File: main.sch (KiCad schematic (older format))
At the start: 0 parts

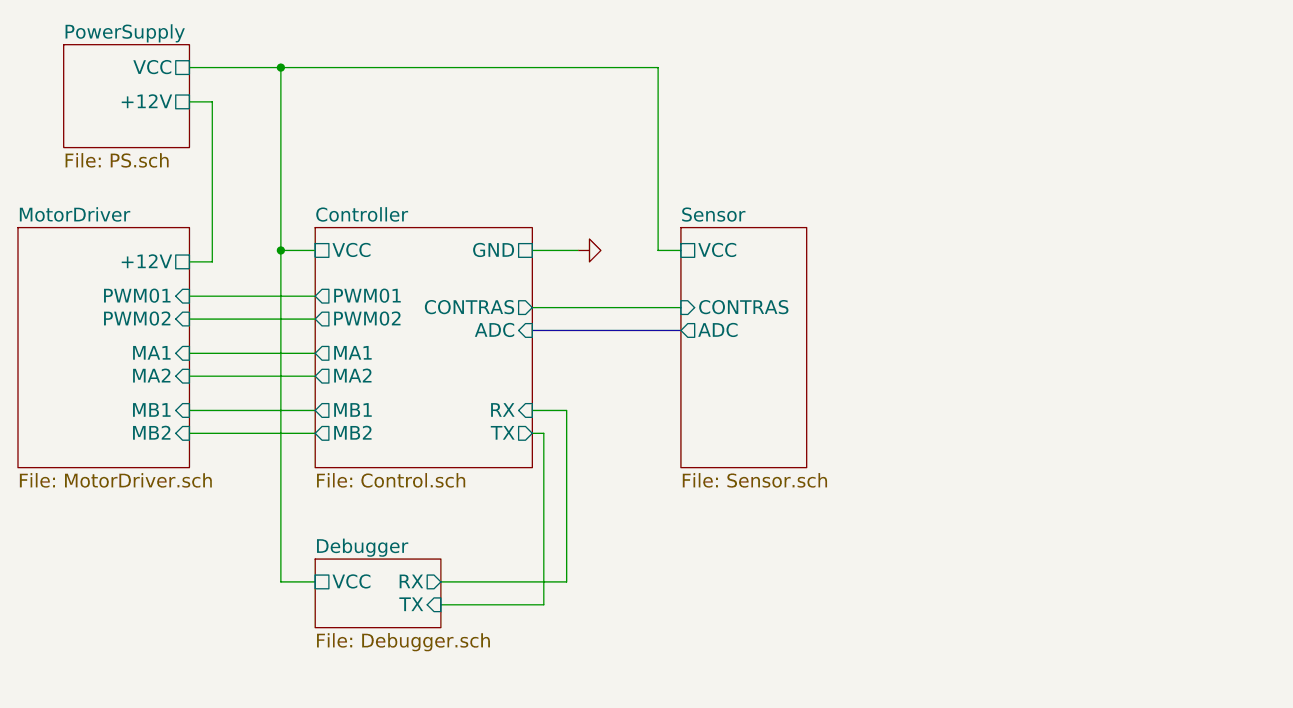
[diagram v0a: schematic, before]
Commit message: Changes to be committed: 	new file:   78LXXSOT89.pdf 	modified:   Control.sch 	modified:   Debugger.sch 	modified:   MotorDriver.sch 	modified:   PS.sch 	modified:   Sensor.sch 	new file:   XL6009-Schematic-Diagram.pdf 	modified:   main-cache.lib 	new file:   main.cmp 	new file:   main.kicad_pcb 	new file:   main.net 	modified:   main.pro 	modified:   main.sch
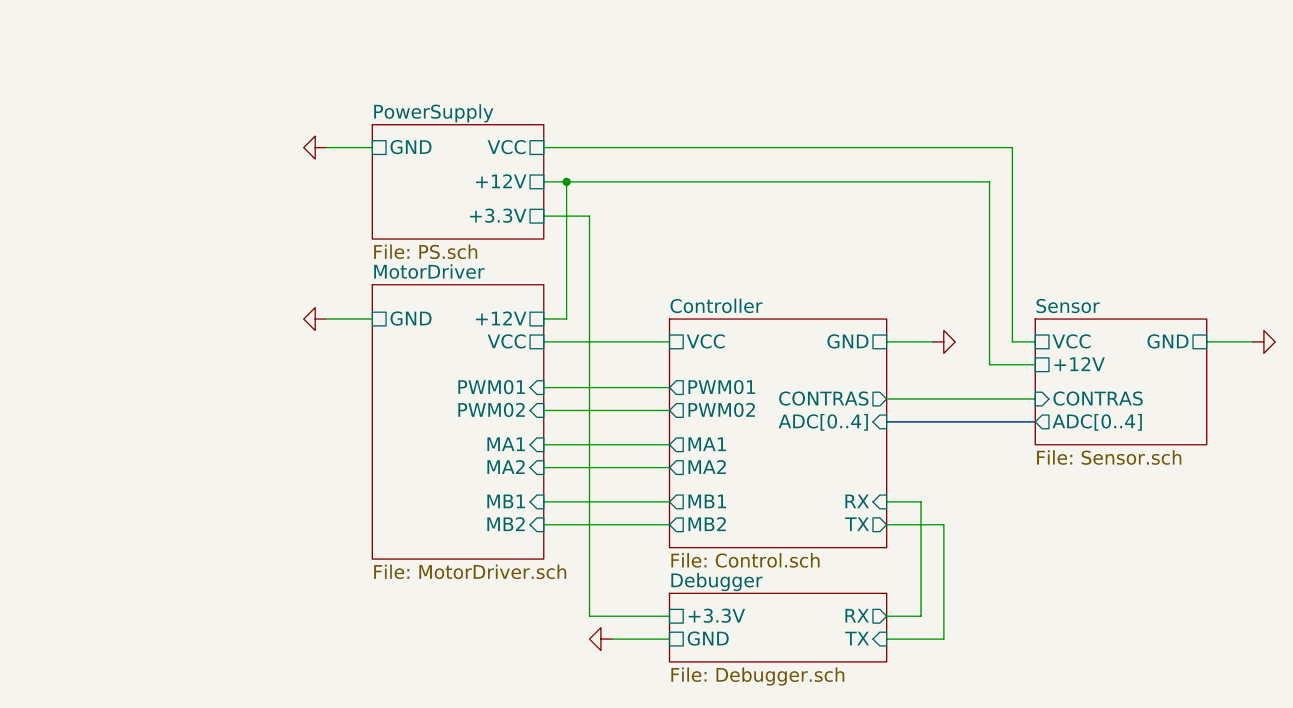
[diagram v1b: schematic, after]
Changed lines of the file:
@@
 EESchema Schematic File Version 2
+LIBS:main-rescue
 LIBS:power
 LIBS:device
@@
 LIBS:contrib
 LIBS:main-cache
+LIBS:tcrt5000
 EELAYER 25 0
 EELAYER END
@@
 $EndDescr
 $Sheet
-S 2650 2550 550  450
+S 4000 3600 750  1200
+U 55880F8C
+F0 "MotorDriver" 60
+F1 "MotorDriver.sch" 60
+F2 "+12V" U R 4750 3750 60
+F3 "PWM01" I R 4750 4050 60
+F4 "MA1" I R 4750 4300 60
+F5 "MA2" I R 4750 4400 60
+F6 "PWM02" I R 4750 4150 60
+F7 "MB1" I R 4750 4550 60
+F8 "MB2" I R 4750 4650 60
+F9 "GND" U L 4000 3750 60
+F10 "VCC" U R 4750 3850 60
+$EndSheet
+$Sheet
+S 5300 3750 950  1000
+U 55880FD4
+F0 "Controller" 60
+F1 "Control.sch" 60
+F2 "PWM01" O L 5300 4050 60
+F3 "PWM02" O L 5300 4150 60
+F4 "RX" I R 6250 4550 60
+F5 "TX" O R 6250 4650 60
+F6 "VCC" U L 5300 3850 60
+F7 "CONTRAS" O R 6250 4100 60
+F8 "MA1" O L 5300 4300 60
+F9 "MA2" O L 5300 4400 60
+F10 "MB1" O L 5300 4550 60
+F11 "MB2" O L 5300 4650 60
+F12 "GND" U R 6250 3850 60
+F13 "ADC[0..4]" I R 6250 4200 60
+$EndSheet
+$Sheet
+S 6900 3750 750  550
+U 55880FEF
+F0 "Sensor" 60
+F1 "Sensor.sch" 60
+F2 "VCC" U L 6900 3850 60
+F3 "CONTRAS" I L 6900 4100 60
+F4 "GND" U R 7650 3850 60
+F5 "+12V" U L 6900 3950 60
+F6 "ADC[0..4]" O L 6900 4200 60
+$EndSheet
+Wire Wire Line
+	4750 3150 6700 3150
+Wire Wire Line
+	6250 5050 6400 5050
+Wire Wire Line
+	6400 5050 6400 4550
+Wire Wire Line
+	6400 4550 6250 4550
+Wire Wire Line
+	6250 4650 6500 4650
+Wire Wire Line
+	6500 4650 6500 5150
+Wire Wire Line
+	6500 5150 6250 5150
+Wire Bus Line
+	6250 4200 6900 4200
+Wire Wire Line
+	6250 4100 6900 4100
+$Comp
+L GND #PWR01
+U 1 1 558D10D4
+P 6450 3850
+F 0 "#PWR01" H 6450 3850 30  0001 C CNN
+F 1 "GND" H 6450 3780 30  0001 C CNN
+F 2 "" H 6450 3850 60  0000 C CNN
+F 3 "" H 6450 3850 60  0000 C CNN
+	1    6450 3850
+	0    -1   -1   0
+$EndComp
+Wire Wire Line
+	6450 3850 6250 3850
+$Comp
+L GND #PWR02
+U 1 1 558CC804
+P 7850 3850
+F 0 "#PWR02" H 7850 3850 30  0001 C CNN
+F 1 "GND" H 7850 3780 30  0001 C CNN
+F 2 "" H 7850 3850 60  0000 C CNN
+F 3 "" H 7850 3850 60  0000 C CNN
+	1    7850 3850
+	0    -1   -1   0
+$EndComp
+Wire Wire Line
+	6700 3950 6900 3950
+Wire Wire Line
+	6700 3150 6700 3950
+$Comp
+L GND #PWR03
+U 1 1 558D142F
+P 3800 3750
+F 0 "#PWR03" H 3800 3750 30  0001 C CNN
+F 1 "GND" H 3800 3680 30  0001 C CNN
+F 2 "" H 3800 3750 60  0000 C CNN
+F 3 "" H 3800 3750 60  0000 C CNN
+	1    3800 3750
+	0    1    1    0
+$EndComp
+Wire Wire Line
+	4000 3750 3800 3750
+Wire Wire Line
+	5300 4550 4750 4550
+Wire Wire Line
+	4750 4650 5300 4650
+Wire Wire Line
+	5300 4400 4750 4400
+Wire Wire Line
+	4750 4300 5300 4300
+Wire Wire Line
+	5300 4050 4750 4050
+Wire Wire Line
+	4750 4150 5300 4150
+Wire Wire Line
+	4750 3750 4850 3750
+Wire Wire Line
+	4850 3750 4850 3150
+Wire Wire Line
+	5300 3850 4750 3850
+Wire Wire Line
+	6800 3850 6900 3850
+Wire Wire Line
+	6800 3000 6800 3850
+$Sheet
+S 4000 2900 750  500
 U 55880F70
 F0 "PowerSupply" 60
 F1 "PS.sch" 60
-F2 "VCC" U R 3200 2650 60
-F3 "+12V" U R 3200 2800 60
-$EndSheet
-$Sheet
-S 2450 3350 750  1050
-U 55880F8C
-F0 "MotorDriver" 60
-F1 "MotorDriver.sch" 60
-F2 "+12V" U R 3200 3500 60
-F3 "PWM01" I R 3200 3650 60
-F4 "MA1" I R 3200 3900 60
-F5 "MA2" I R 3200 4000 60
-F6 "PWM02" I R 3200 3750 60
-F7 "MB1" I R 3200 4150 60
-F8 "MB2" I R 3200 4250 60
-$EndSheet
-$Sheet
-S 3750 3350 950  1050
-U 55880FD4
-F0 "Controller" 60
-F1 "Control.sch" 60
-F2 "PWM01" O L 3750 3650 60
-F3 "PWM02" O L 3750 3750 60
-F4 "RX" I R 4700 4150 60
-F5 "TX" O R 4700 4250 60
-F6 "VCC" U L 3750 3450 60
-F7 "ADC" I R 4700 3800 60
-F8 "CONTRAS" O R 4700 3700 60
-F9 "MA1" O L 3750 3900 60
-F10 "MA2" O L 3750 4000 60
-F11 "MB1" O L 3750 4150 60
-F12 "MB2" O L 3750 4250 60
-F13 "GND" U R 4700 3450 60
-$EndSheet
-$Sheet
-S 5350 3350 550  1050
-U 55880FEF
-F0 "Sensor" 60
-F1 "Sensor.sch" 60
-F2 "ADC" O L 5350 3800 60
-F3 "VCC" U L 5350 3450 60
-F4 "CONTRAS" I L 5350 3700 60
-$EndSheet
-$Sheet
-S 3750 4800 550  300
+F2 "VCC" U R 4750 3000 60
+F3 "+12V" U R 4750 3150 60
+F4 "GND" U L 4000 3000 60
+F5 "+3.3V" U R 4750 3300 60
+$EndSheet
+Wire Wire Line
+	4750 3000 6800 3000
+Connection ~ 4850 3150
+$Comp
+L GND #PWR04
+U 1 1 558E0147
+P 3800 3000
+F 0 "#PWR04" H 3800 3000 30  0001 C CNN
+F 1 "GND" H 3800 2930 30  0001 C CNN
+F 2 "" H 3800 3000 60  0000 C CNN
+F 3 "" H 3800 3000 60  0000 C CNN
+	1    3800 3000
+	0    1    1    0
+$EndComp
+Wire Wire Line
+	4000 3000 3800 3000
+Wire Wire Line
+	5300 5050 4950 5050
+Wire Wire Line
+	4950 5050 4950 3300
+Wire Wire Line
+	4950 3300 4750 3300
+Wire Wire Line
+	7650 3850 7850 3850
+$Sheet
+S 5300 4950 950  300
 U 558810F4
 F0 "Debugger" 60
 F1 "Debugger.sch" 60
-F2 "RX" O R 4300 4900 60
-F3 "TX" I R 4300 5000 60
-F4 "VCC" U L 3750 4900 60
-$EndSheet
-Wire Wire Line
-	3600 3450 3750 3450
-Wire Wire Line
-	3750 3650 3200 3650
-Wire Wire Line
-	3200 3750 3750 3750
-Wire Wire Line
-	3750 3900 3200 3900
-Wire Wire Line
-	3200 4000 3750 4000
-Wire Wire Line
-	3750 4150 3200 4150
-Wire Wire Line
-	3200 4250 3750 4250
-Wire Wire Line
-	3200 3500 3300 3500
-Wire Wire Line
-	3300 3500 3300 2800
-Wire Wire Line
-	3300 2800 3200 2800
-Wire Wire Line
-	3200 2650 5250 2650
-Wire Wire Line
-	3600 2650 3600 4900
-Wire Wire Line
-	3600 4900 3750 4900
-Connection ~ 3600 3450
-Wire Wire Line
-	4300 4900 4850 4900
-Wire Wire Line
-	4850 4900 4850 4150
-Wire Wire Line
-	4850 4150 4700 4150
-Wire Wire Line
-	4700 4250 4750 4250
-Wire Wire Line
-	4750 4250 4750 5000
-Wire Wire Line
-	4750 5000 4300 5000
-Wire Bus Line
-	4700 3800 5350 3800
-Wire Wire Line
-	4700 3700 5350 3700
-Wire Wire Line
-	5350 3450 5250 3450
-Wire Wire Line
-	5250 3450 5250 2650
-Connection ~ 3600 2650
-$Comp
-L GND #PWR01
-U 1 1 558D10D4
-P 4900 3450
-F 0 "#PWR01" H 4900 3450 30  0001 C CNN
-F 1 "GND" H 4900 3380 30  0001 C CNN
-F 2 "" H 4900 3450 60  0000 C CNN
-F 3 "" H 4900 3450 60  0000 C CNN
-	1    4900 3450
-	0    -1   -1   0
-$EndComp
-Wire Wire Line
-	4900 3450 4700 3450
+F2 "RX" O R 6250 5050 60
+F3 "TX" I R 6250 5150 60
+F4 "+3.3V" U L 5300 5050 60
+F5 "GND" U L 5300 5150 60
+$EndSheet
+$Comp
+L GND #PWR05
+U 1 1 558E5B9D
+P 5050 5150
+F 0 "#PWR05" H 5050 5150 30  0001 C CNN
+F 1 "GND" H 5050 5080 30  0001 C CNN
+F 2 "" H 5050 5150 60  0000 C CNN
+F 3 "" H 5050 5150 60  0000 C CNN
+	1    5050 5150
+	0    1    1    0
+$EndComp
+Wire Wire Line
+	5300 5150 5050 5150
 $EndSCHEMATC

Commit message: update
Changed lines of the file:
@@
 LIBS:memory
 LIBS:xilinx
-LIBS:special
 LIBS:microcontrollers
 LIBS:dsp
@@
 encoding utf-8
 Sheet 1 6
-Title ""
-Date ""
-Rev ""
+Title "KENZANIN LINEFOLLOWER"
+Date "2015-06-28"
+Rev "1.0"
 Comp ""
 Comment1 ""
@@
 Wire Wire Line
 	5300 5150 5050 5150
+Connection ~ 5200 3850
+Wire Wire Line
+	5200 3850 5200 3000
+Connection ~ 5200 3000
 $EndSCHEMATC
